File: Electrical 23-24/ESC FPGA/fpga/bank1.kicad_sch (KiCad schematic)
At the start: 14 parts, among them J2 LSHM-110-04.0-L-DV-A-N-K-TR, J4 LSHM-110-04.0-L-DV-A-N-K-TR, SW1 SW_SPDT, U1 XC6SLX4-TQG144, U13 FXMA108BQX, U14 FXMA108BQX

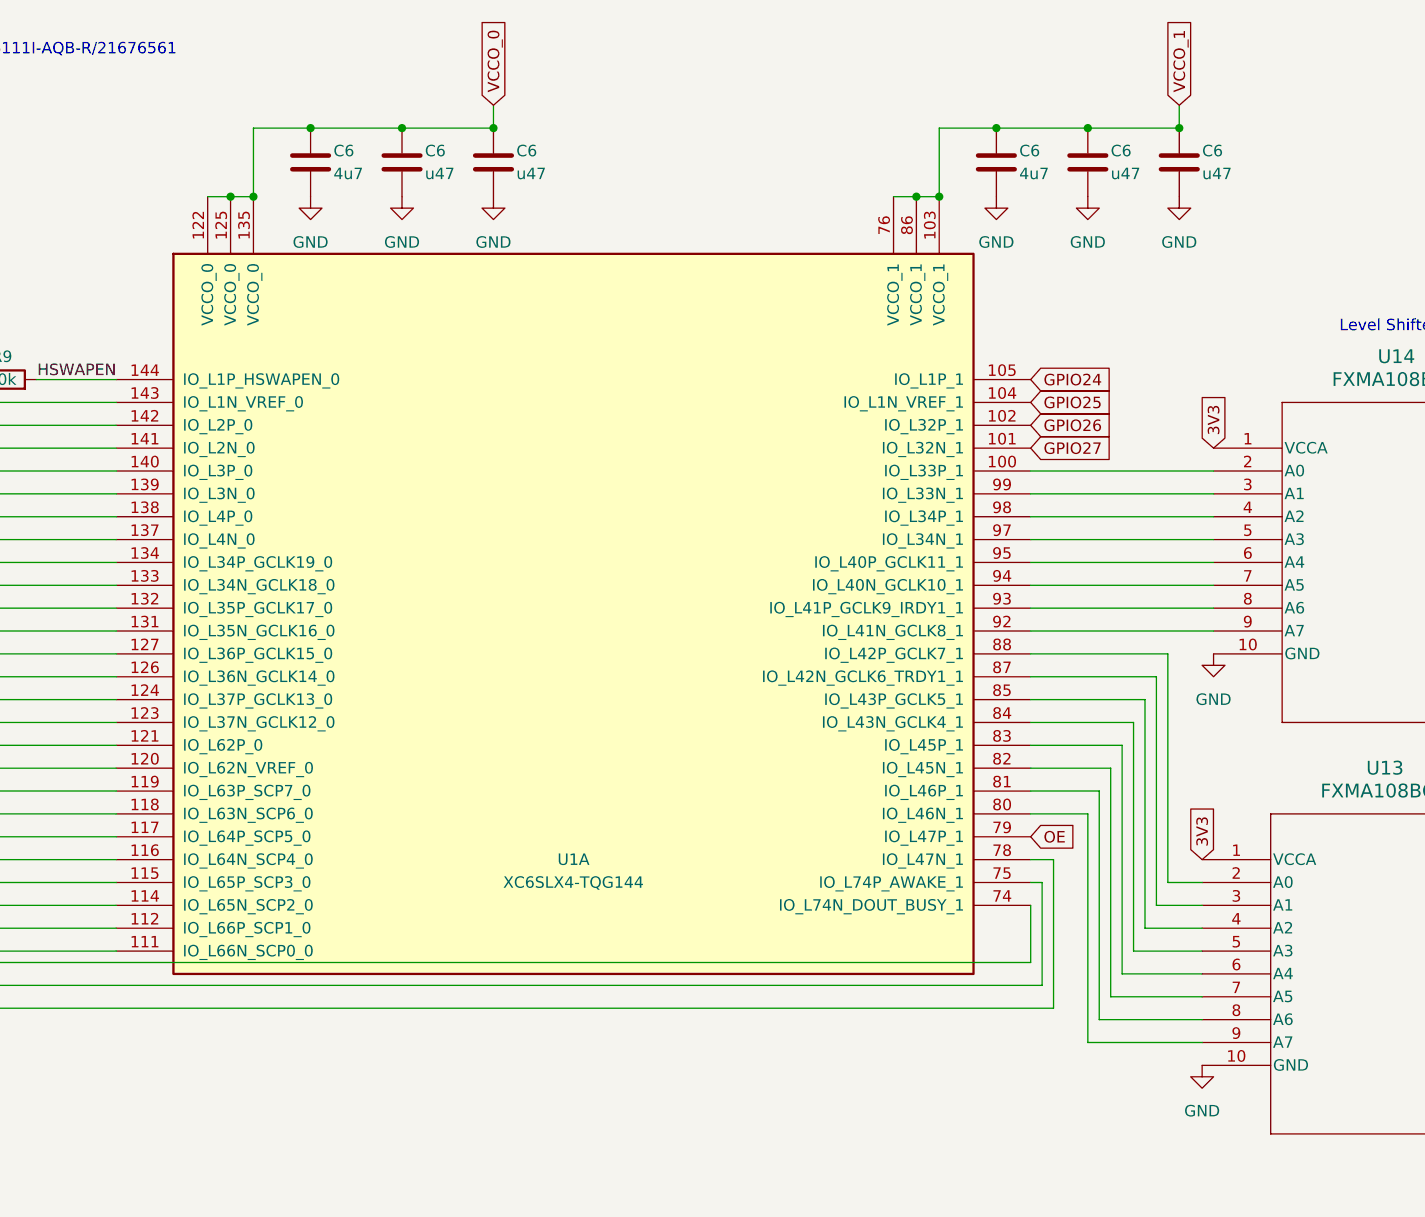
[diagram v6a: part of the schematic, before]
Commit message: Made BOM, need to modify footprints
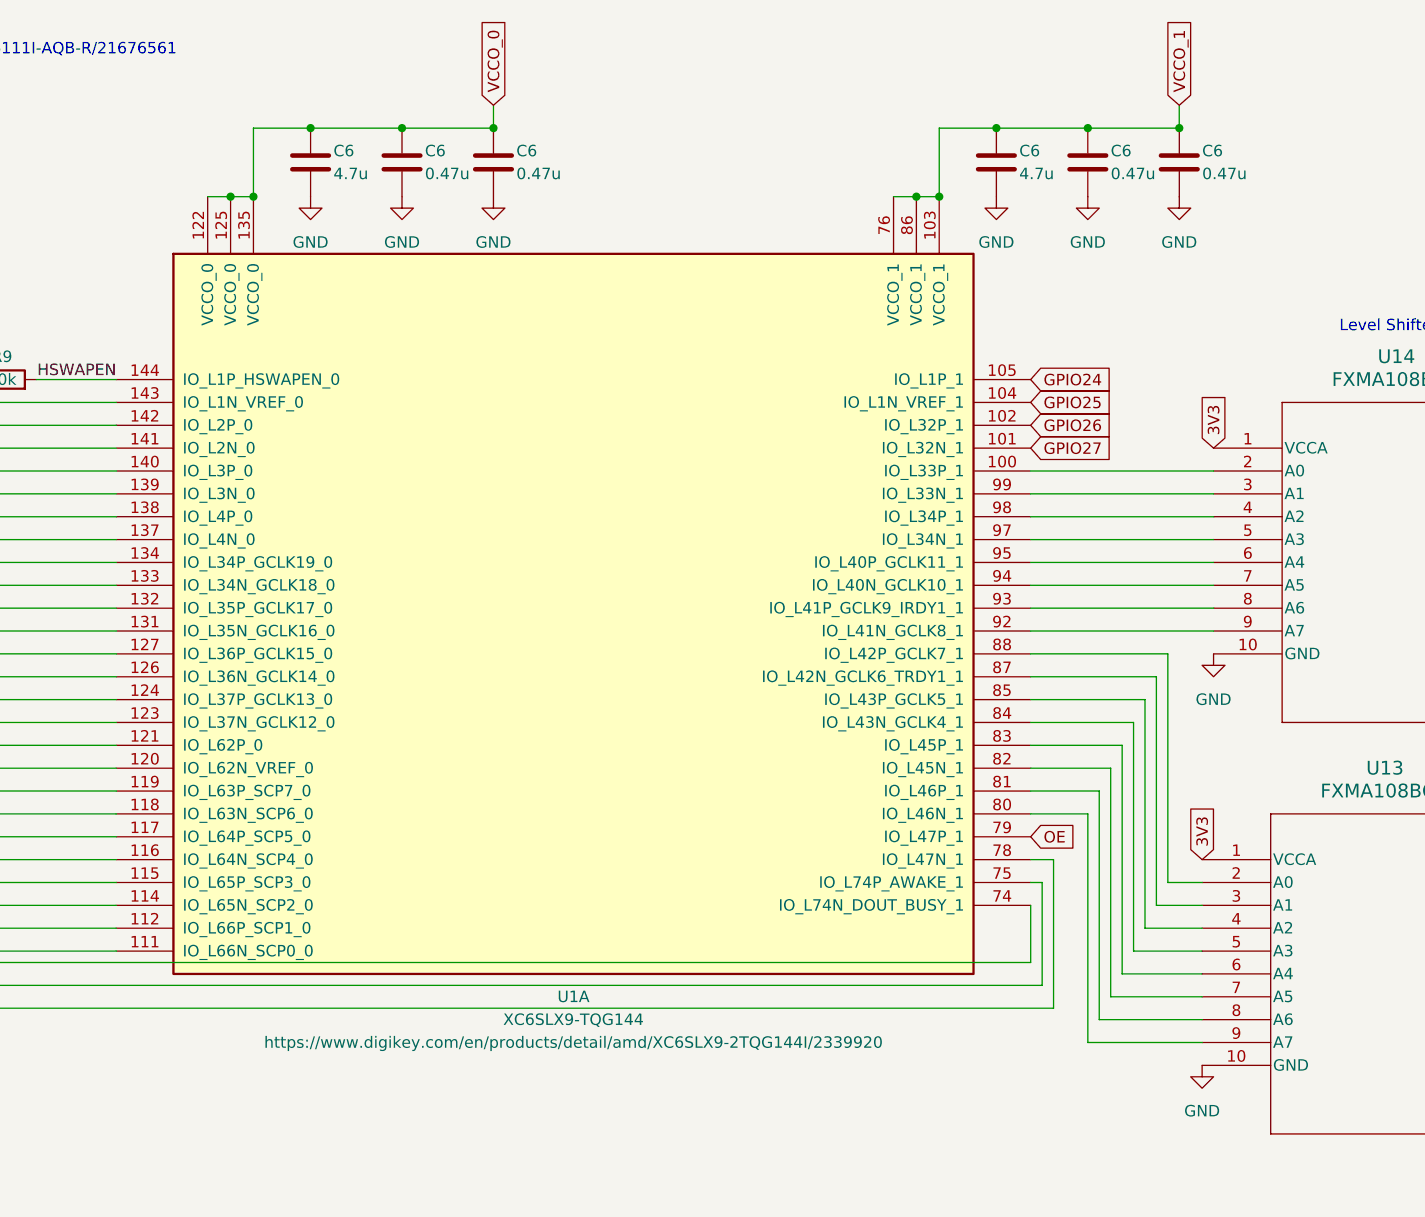
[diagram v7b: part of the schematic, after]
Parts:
- removed SW1 (x2): SW_SPDT, symbol Switch:SW_SPDT
- removed U1: XC6SLX4-TQG144, symbol FPGA_Xilinx_Spartan6:XC6SLX4-TQG144
- added SW1 (x2): SW_SPDT, Connector_PinHeader_2.54mm:PinHeader_1x03_P2.54mm_Vertical, symbol Switch:SW_SPDT
- added U1: XC6SLX9-TQG144, fpga:TQFP-144_20x20mm_P0.5mm, symbol FPGA_Xilinx_Spartan6:XC6SLX9-TQG144
- C6: value 4u7 -> 4.7u; footprint (none) -> Capacitor_SMD:C_0402_1005Metric_Pad0.74x0.62mm_HandSolder
- C6: value u47 -> 0.47u; footprint (none) -> Capacitor_SMD:C_0402_1005Metric_Pad0.74x0.62mm_HandSolder
- J2, J4: footprint LSHM-110-04.0-L-DV-A-N-K-TR:SAMTEC_LSHM-110-04.0-L-DV-A-N-K-TR -> fpga:SAMTEC_LSHM-110-04.0-L-DV-A-N-K-TR; Digi (none) -> https://www.digikey.com/en/products/detail/samtec-inc/LSHM-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
- R9: footprint (none) -> Resistor_SMD:R_0402_1005Metric_Pad0.72x0.64mm_HandSolder
- U13, U14: footprint WQFN20_2P5X4P5_ONS -> fpga:WQFN20_2P5X4P5_ONS
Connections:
- net 3V3: now also SW1.3 (C), SW1.3 (C)
- net GPIO24: now also U1.105 (IO_L1P_1)
- net GPIO25: now also U1.104 (IO_L1N_VREF_1)
- net GPIO26: now also U1.102 (IO_L32P_1)
- net GPIO27: now also U1.101 (IO_L32N_1)
- net HSWAPEN: now also U1.144 (IO_L1P_HSWAPEN_0)
- net OE: now also U1.79 (IO_L47P_1)
- net VCCO_0: now also U1.122 (VCCO_0), U1.125 (VCCO_0), U1.135 (VCCO_0)
- net VCCO_1: now also U1.103 (VCCO_1), U1.76 (VCCO_1), U1.86 (VCCO_1)
- net VUSB: now also SW1.1 (A), SW1.1 (A)
- net at U13.2 (A0): now also U1.88 (IO_L42P_GCLK7_1)
- net at U13.20 (VCCB): now also SW1.2 (B)
- net at U13.3 (A1): now also U1.87 (IO_L42N_GCLK6_TRDY1_1)
- net at U13.4 (A2): now also U1.85 (IO_L43P_GCLK5_1)
- net at U13.5 (A3): now also U1.84 (IO_L43N_GCLK4_1)
- net at U13.6 (A4): now also U1.83 (IO_L45P_1)
- net at U13.7 (A5): now also U1.82 (IO_L45N_1)
- net at U13.8 (A6): now also U1.81 (IO_L46P_1)
- net at U13.9 (A7): now also U1.80 (IO_L46N_1)
- net at J2.02: now also U1.143 (IO_L1N_VREF_0)
- net at J2.04: now also U1.142 (IO_L2P_0)
- net at J2.06: now also U1.141 (IO_L2N_0)
- net at J2.08: now also U1.140 (IO_L3P_0)
- net at J2.10: now also U1.139 (IO_L3N_0)
- net at J2.12: now also U1.138 (IO_L4P_0)
- net at J2.13: now also U1.124 (IO_L37P_GCLK13_0)
- net at J2.14: now also U1.137 (IO_L4N_0)
- net at J2.15: now also U1.126 (IO_L36N_GCLK14_0)
- net at J2.16: now also U1.134 (IO_L34P_GCLK19_0)
- net at J2.17: now also U1.127 (IO_L36P_GCLK15_0)
- net at J2.18: now also U1.133 (IO_L34N_GCLK18_0)
- net at J2.19: now also U1.131 (IO_L35N_GCLK16_0)
- net at J2.20: now also U1.132 (IO_L35P_GCLK17_0)
- net at U14.20 (VCCB): now also SW1.2 (B)
- net at U14.2 (A0): now also U1.100 (IO_L33P_1)
- net at J4.19: now also U1.111 (IO_L66N_SCP0_0)
- net at J4.20: now also U1.112 (IO_L66P_SCP1_0)
- net at J4.18: now also U1.114 (IO_L65N_SCP2_0)
- net at J4.16: now also U1.115 (IO_L65P_SCP3_0)
- net at J4.14: now also U1.116 (IO_L64N_SCP4_0)
- net at J4.12: now also U1.117 (IO_L64P_SCP5_0)
- net at J4.10: now also U1.118 (IO_L63N_SCP6_0)
- net at J4.08: now also U1.119 (IO_L63P_SCP7_0)
- net at J4.06: now also U1.120 (IO_L62N_VREF_0)
- net at J4.04: now also U1.121 (IO_L62P_0)
- net at J4.02: now also U1.123 (IO_L37N_GCLK12_0)
- net at J4.17: now also U1.74 (IO_L74N_DOUT_BUSY_1)
- net at J4.15: now also U1.75 (IO_L74P_AWAKE_1)
- net at J4.13: now also U1.78 (IO_L47N_1)
- net at U14.9 (A7): now also U1.92 (IO_L41N_GCLK8_1)
- net at U14.8 (A6): now also U1.93 (IO_L41P_GCLK9_IRDY1_1)
- net at U14.7 (A5): now also U1.94 (IO_L40N_GCLK10_1)
- net at U14.6 (A4): now also U1.95 (IO_L40P_GCLK11_1)
- net at U14.5 (A3): now also U1.97 (IO_L34N_1)
- net at U14.4 (A2): now also U1.98 (IO_L34P_1)
- net at U14.3 (A1): now also U1.99 (IO_L33N_1)

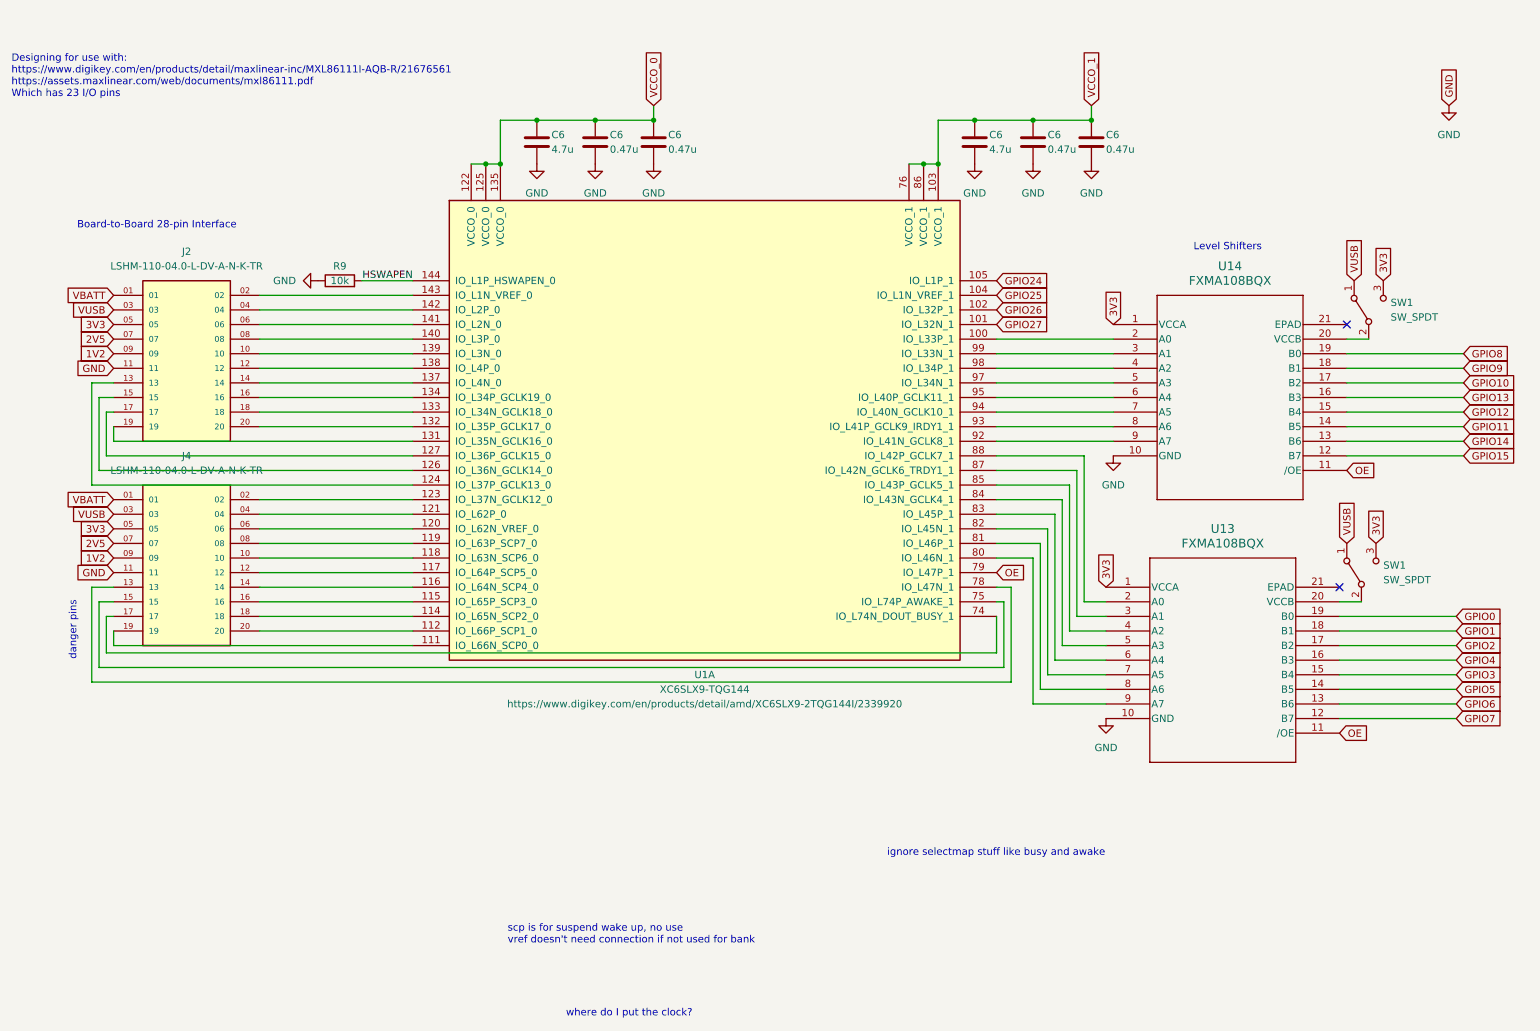
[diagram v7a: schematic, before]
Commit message: Finished hard signal routing, need PMOD and Power
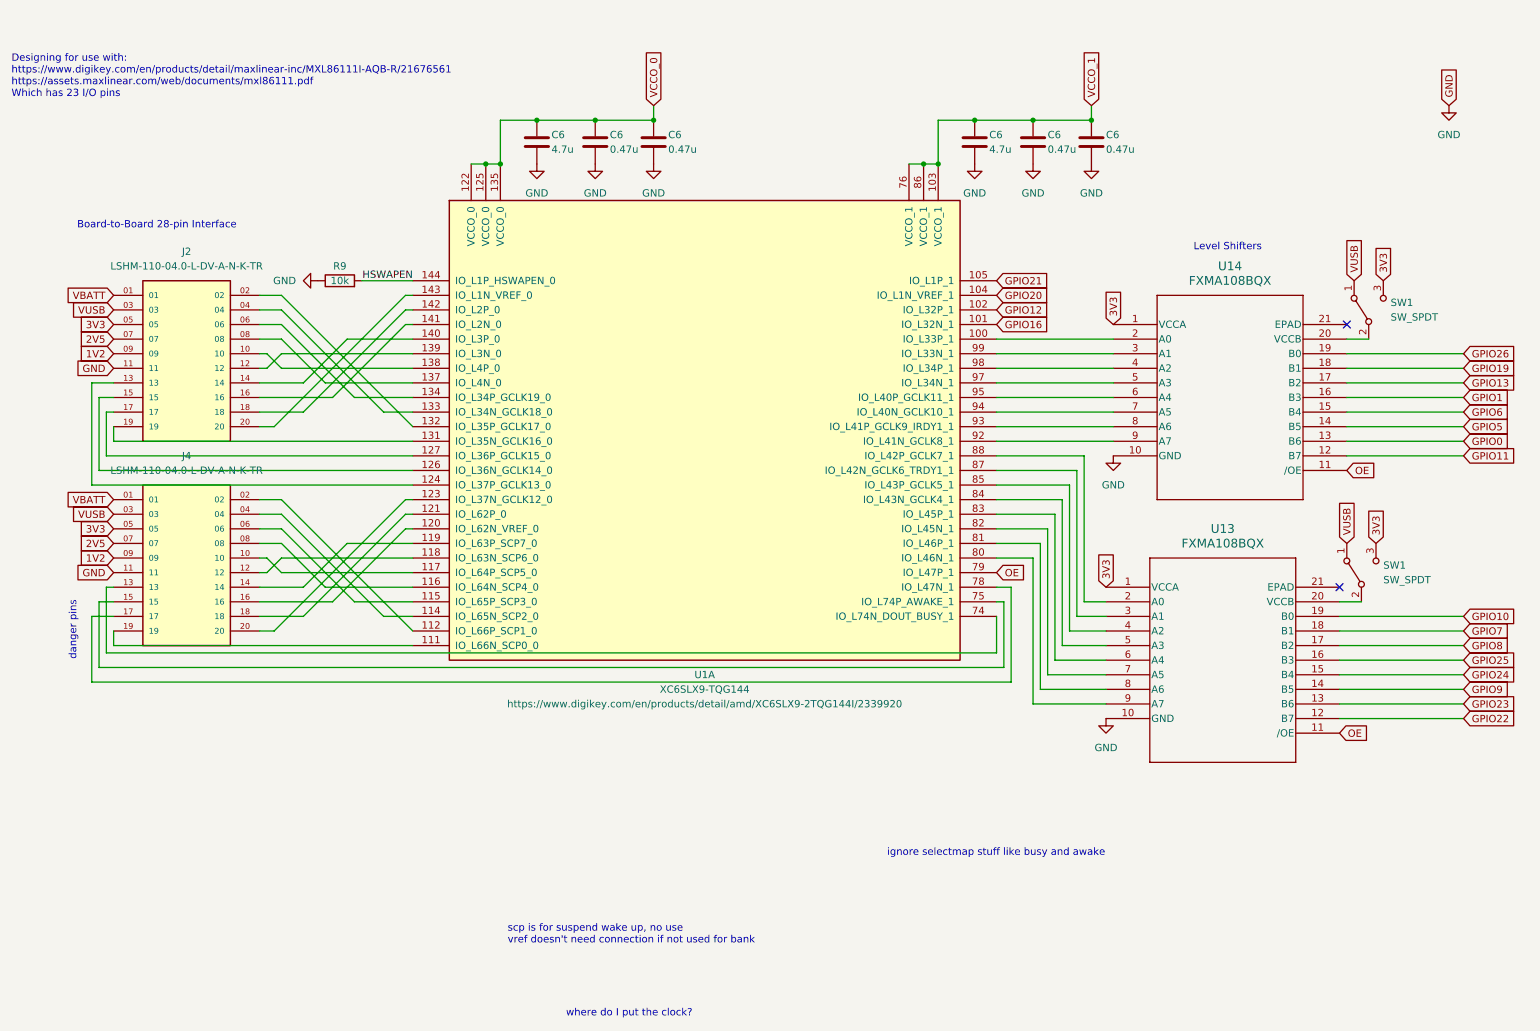
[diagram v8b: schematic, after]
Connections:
- net GPIO14 is gone; now on net GPIO0: U14.13 (B6)
- net GPIO15 is gone; now on net GPIO11: U14.12 (B7)
- net GPIO2 is gone; now on net GPIO8: U13.17 (B2)
- net GPIO3 is gone; now on net GPIO24: U13.15 (B4)
- net GPIO4 is gone; now on net GPIO25: U13.16 (B3)
- net GPIO0: no longer U13.19 (B0)
- net GPIO1: now also U14.16 (B3); no longer U13.18 (B1)
- net GPIO10: now also U13.19 (B0); no longer U14.17 (B2)
- net GPIO11: no longer U14.14 (B5)
- net GPIO12: now also U1.102 (IO_L32P_1); no longer U14.15 (B4)
- net GPIO13: now also U14.17 (B2); no longer U14.16 (B3)
- net GPIO24: no longer U1.105 (IO_L1P_1)
- net GPIO25: no longer U1.104 (IO_L1N_VREF_1)
- net GPIO26: now also U14.19 (B0); no longer U1.102 (IO_L32P_1)
- net GPIO5: now also U14.14 (B5); no longer U13.14 (B5)
- net GPIO6: now also U14.15 (B4); no longer U13.13 (B6)
- net GPIO7: now also U13.18 (B1); no longer U13.12 (B7)
- net GPIO8: no longer U14.19 (B0)
- net GPIO9: now also U13.14 (B5); no longer U14.18 (B1)
- net at U1.112 (IO_L66P_SCP1_0): now also J4.02; no longer J4.20
- net at U1.114 (IO_L65N_SCP2_0): now also J4.04; no longer J4.18
- net at U1.115 (IO_L65P_SCP3_0): now also J4.06; no longer J4.16
- net at U1.116 (IO_L64N_SCP4_0): now also J4.08; no longer J4.14
- net at U1.117 (IO_L64P_SCP5_0): now also J4.10; no longer J4.12
- net at U1.118 (IO_L63N_SCP6_0): now also J4.12; no longer J4.10
- net at U1.119 (IO_L63P_SCP7_0): now also J4.14; no longer J4.08
- net at U1.120 (IO_L62N_VREF_0): now also J4.16; no longer J4.06
- net at U1.121 (IO_L62P_0): now also J4.18; no longer J4.04
- net at U1.123 (IO_L37N_GCLK12_0): now also J4.20; no longer J4.02
- net at U1.132 (IO_L35P_GCLK17_0): now also J2.02; no longer J2.20
- net at U1.133 (IO_L34N_GCLK18_0): now also J2.04; no longer J2.18
- net at U1.134 (IO_L34P_GCLK19_0): now also J2.06; no longer J2.16
- net at U1.137 (IO_L4N_0): now also J2.08; no longer J2.14
- net at U1.138 (IO_L4P_0): now also J2.10; no longer J2.12
- net at U1.139 (IO_L3N_0): now also J2.12; no longer J2.10
- net at U1.140 (IO_L3P_0): now also J2.14; no longer J2.08
- net at U1.141 (IO_L2N_0): now also J2.16; no longer J2.06
- net at U1.142 (IO_L2P_0): now also J2.18; no longer J2.04
- net at U1.143 (IO_L1N_VREF_0): now also J2.20; no longer J2.02
- net at U1.74 (IO_L74N_DOUT_BUSY_1): now also J4.13; no longer J4.17
- net at U1.78 (IO_L47N_1): now also J4.17; no longer J4.13
- net GPIO27 renamed GPIO16
- new net GPIO19: U14.18 (B1)
- new net GPIO20: U1.104 (IO_L1N_VREF_1)
- new net GPIO21: U1.105 (IO_L1P_1)
- new net GPIO22: U13.12 (B7)
- new net GPIO23: U13.13 (B6)
